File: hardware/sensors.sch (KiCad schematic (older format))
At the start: 22 parts

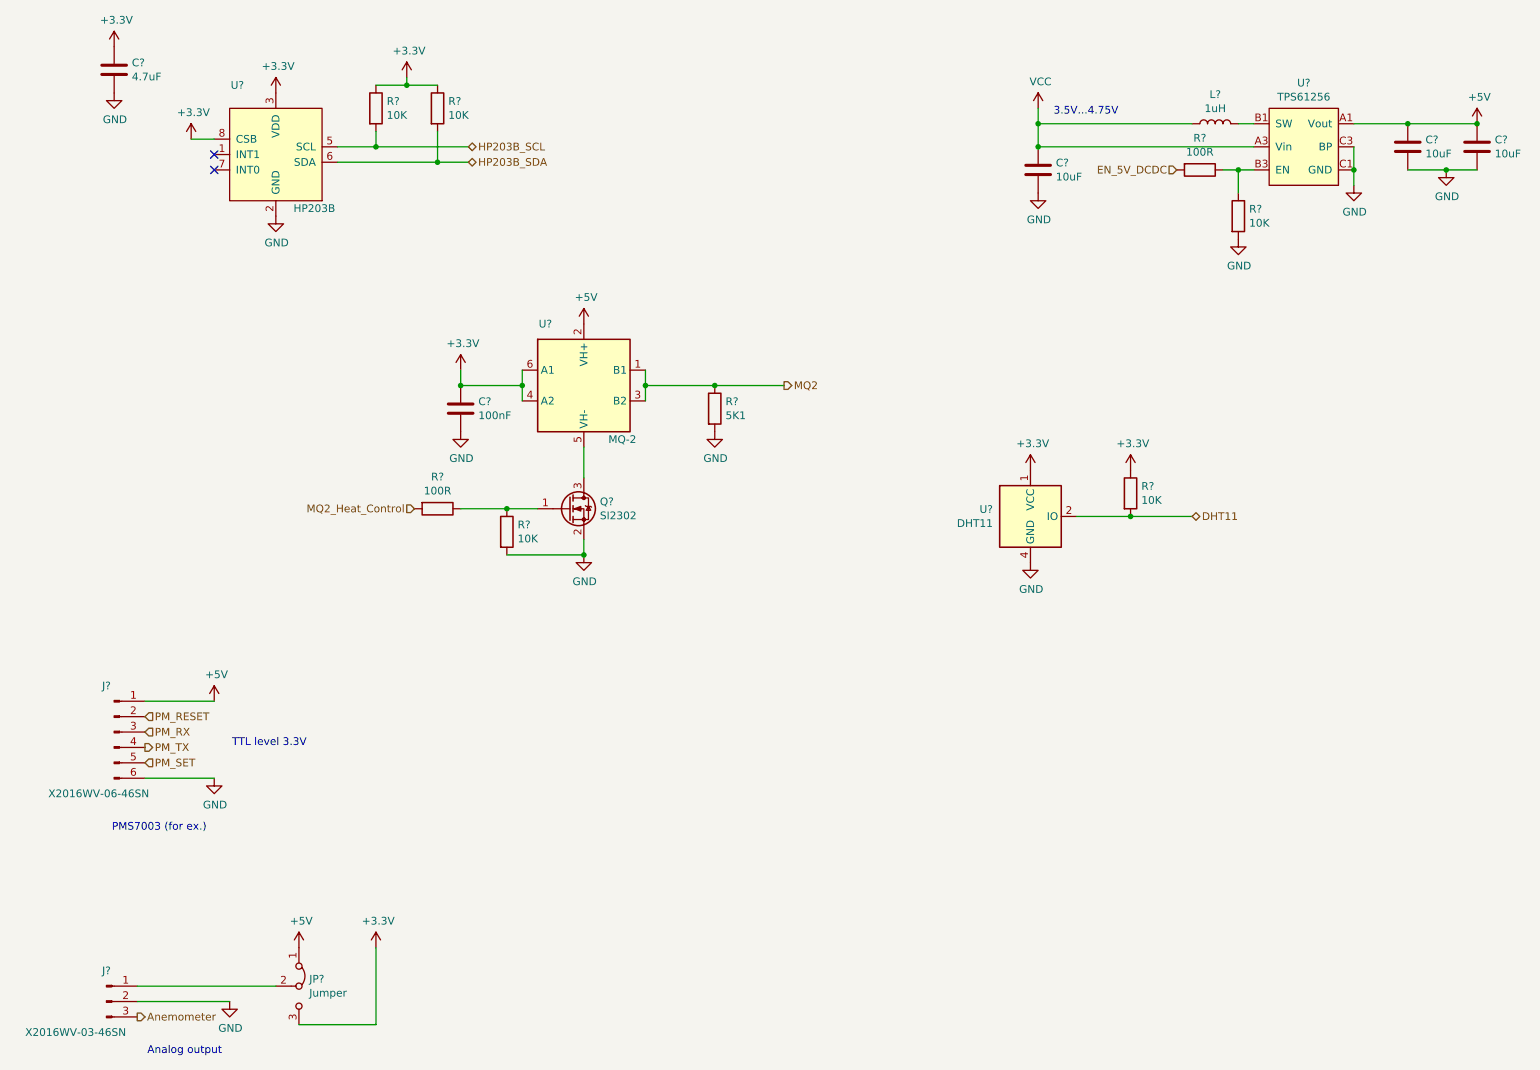
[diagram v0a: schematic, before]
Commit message: Select crystals, add HSE for stm32 and fixed some bits
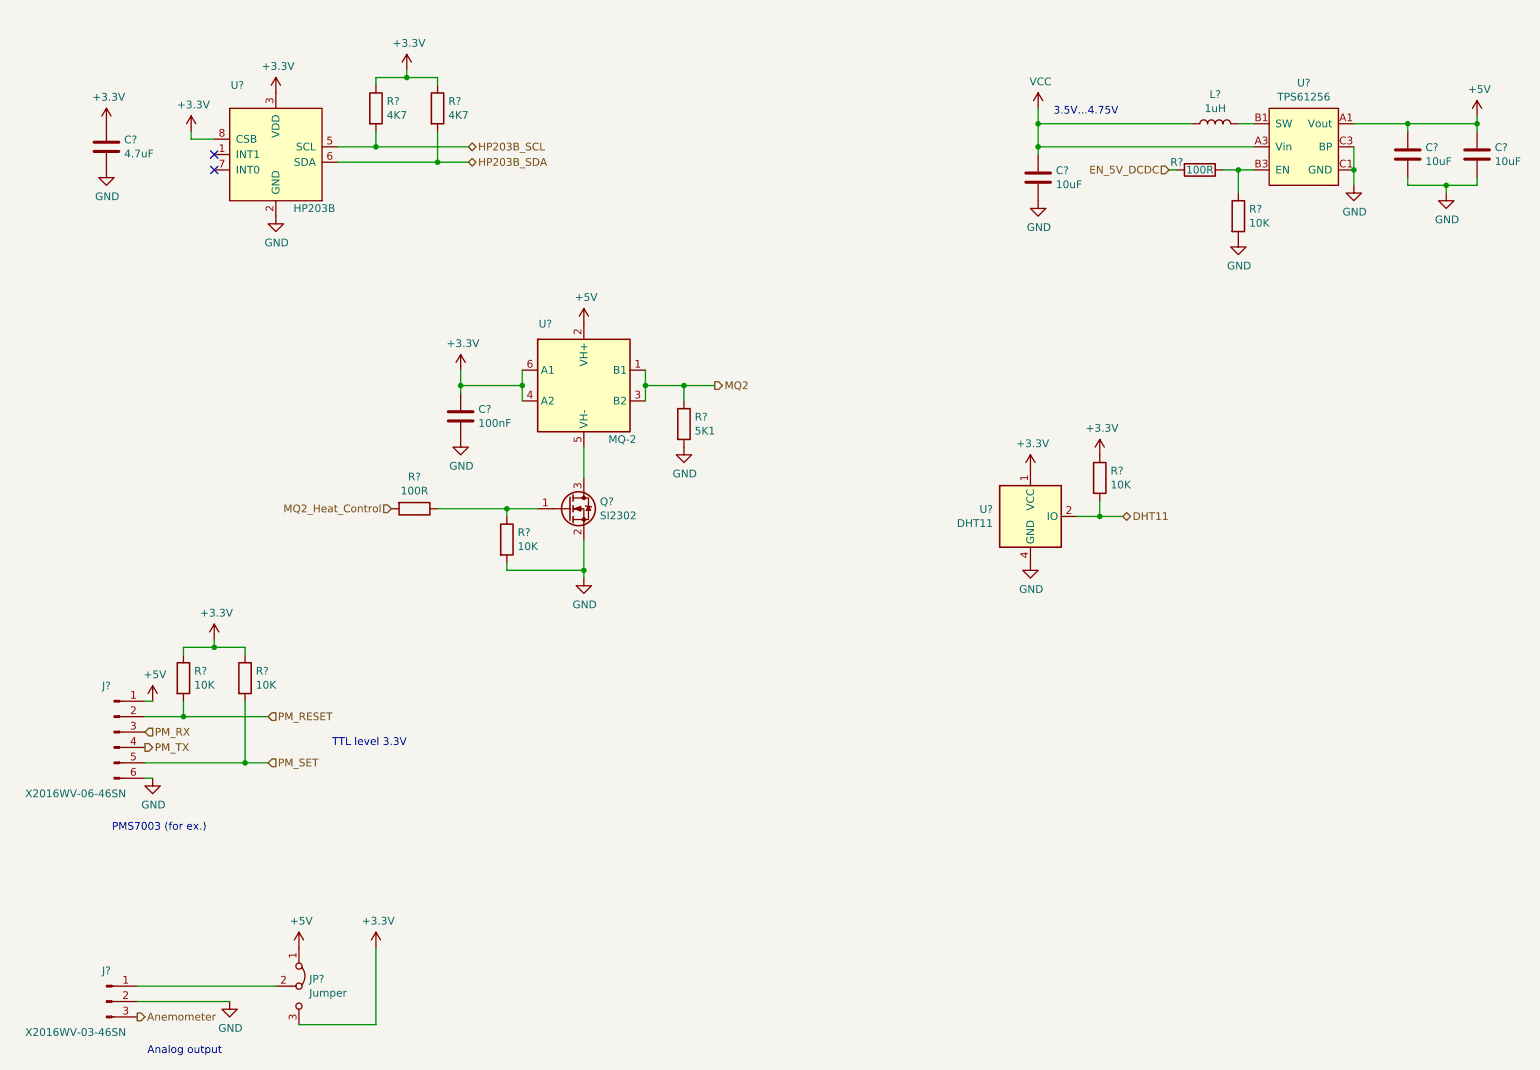
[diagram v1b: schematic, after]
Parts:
- added R? (x2): 10K, symbol Device:R
- R? (x2): value 10K -> 4K7
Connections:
- net +3V3: now also R?.1, R?.1
- net PM_RESET: now also R?.2
- net PM_SET: now also R?.2
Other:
- moved on the sheet: C?, R?

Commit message: Annotation complete
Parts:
- gave numbers to parts that had none: 24

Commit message: Finish adding footprints
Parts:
- removed U011: TPS61256, Package_BGA:Texas_DSBGA-9_1.4715x1.4715mm_Layout3x3_P0.5mm, symbol TPS61256:TPS61256
- C60, C61, C62, C63, C64: footprint (none) -> Capacitor_SMD:C_0805_2012Metric
- J3: value X2016WV-06-46SN -> PM_Sensor; footprint (none) -> Connector_PinSocket_2.00mm:PinSocket_1x06_P2.00mm_Vertical
- J4: value X2016WV-03-46SN -> Anemometer; footprint (none) -> Connector_PinSocket_2.00mm:PinSocket_1x03_P2.00mm_Vertical
- JP3: footprint (none) -> Connector_PinHeader_2.54mm:PinHeader_1x03_P2.54mm_Vertical
- L12: footprint (none) -> Inductor_SMD:L_0603_1608Metric
- R54, R55, R56, R57, R58, R59, R60, R61, R62, R63: footprint (none) -> Resistor_SMD:R_0805_2012Metric
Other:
- moved on the sheet: C63, R56
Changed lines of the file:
@@
 $EndComp
 $Comp
-L TPS61256:TPS61256 U011
+L TPS61256:TPS61256 #U011
 U 1 1 6059B871
 P 9050 1750
-F 0 "U011" H 9075 2165 50  0000 C CNN
+F 0 "#U011" H 9075 2165 50  0000 C CNN
 F 1 "TPS61256" H 9075 2074 50  0000 C CNN
 F 2 "Package_BGA:Texas_DSBGA-9_1.4715x1.4715mm_Layout3x3_P0.5mm" H 9050 2100 50  0001 C CNN
@@
 L power:VCC #PWR0105
 U 1 1 6059CBA1
-P 7350 1500
-F 0 "#PWR0105" H 7350 1350 50  0001 C CNN
-F 1 "VCC" H 7365 1673 50  0000 C CNN
-F 2 "" H 7350 1500 50  0001 C CNN
-F 3 "" H 7350 1500 50  0001 C CNN
-	1    7350 1500
+P 7200 1500
+F 0 "#PWR0105" H 7200 1350 50  0001 C CNN
+F 1 "VCC" H 7215 1673 50  0000 C CNN
+F 2 "" H 7200 1500 50  0001 C CNN
+F 3 "" H 7200 1500 50  0001 C CNN
+	1    7200 1500
 	1    0    0    -1
 $EndComp
@@
 F 0 "L12" V 8690 1600 50  0000 C CNN
 F 1 "1uH" V 8599 1600 50  0000 C CNN
-F 2 "" H 8500 1600 50  0001 C CNN
+F 2 "Inductor_SMD:L_0603_1608Metric" H 8500 1600 50  0001 C CNN
 F 3 "~" H 8500 1600 50  0001 C CNN
 	1    8500 1600
@@
 L Device:C C63
 U 1 1 6059E1D4
-P 7350 1950
-F 0 "C63" H 7465 1996 50  0000 L CNN
-F 1 "10uF" H 7465 1905 50  0000 L CNN
-F 2 "" H 7388 1800 50  0001 C CNN
-F 3 "~" H 7350 1950 50  0001 C CNN
-	1    7350 1950
+P 7200 1950
+F 0 "C63" H 7315 1996 50  0000 L CNN
+F 1 "10uF" H 7315 1905 50  0000 L CNN
+F 2 "Capacitor_SMD:C_0805_2012Metric" H 7238 1800 50  0001 C CNN
+F 3 "~" H 7200 1950 50  0001 C CNN
+	1    7200 1950
 	1    0    0    -1
 $EndComp
@@
 L power:GND #PWR0112
 U 1 1 605A030F
-P 7350 2100
-F 0 "#PWR0112" H 7350 1850 50  0001 C CNN
-F 1 "GND" H 7355 1927 50  0000 C CNN
-F 2 "" H 7350 2100 50  0001 C CNN
-F 3 "" H 7350 2100 50  0001 C CNN
-	1    7350 2100
+P 7200 2100
+F 0 "#PWR0112" H 7200 1850 50  0001 C CNN
+F 1 "GND" H 7205 1927 50  0000 C CNN
+F 2 "" H 7200 2100 50  0001 C CNN
+F 3 "" H 7200 2100 50  0001 C CNN
+	1    7200 2100
 	1    0    0    -1
 $EndComp
@@
 F 0 "C61" H 9865 1846 50  0000 L CNN
 F 1 "10uF" H 9865 1755 50  0000 L CNN
-F 2 "" H 9788 1650 50  0001 C CNN
+F 2 "Capacitor_SMD:C_0805_2012Metric" H 9788 1650 50  0001 C CNN
 F 3 "~" H 9750 1800 50  0001 C CNN
 	1    9750 1800
@@
 F 0 "C62" H 10315 1846 50  0000 L CNN
 F 1 "10uF" H 10315 1755 50  0000 L CNN
-F 2 "" H 10238 1650 50  0001 C CNN
+F 2 "Capacitor_SMD:C_0805_2012Metric" H 10238 1650 50  0001 C CNN
 F 3 "~" H 10200 1800 50  0001 C CNN
 	1    10200 1800
@@
 	1    0    0    -1
 $EndComp
-Text HLabel 8200 1900 0    50   Input ~ 0
+Text HLabel 8150 1900 0    50   Input ~ 0
 EN_5V_DCDC
 Wire Wire Line
-	7350 1750 7350 1600
-Connection ~ 7350 1750
-Connection ~ 7350 1600
-Wire Wire Line
-	7350 1600 7350 1500
+	7200 1750 7200 1600
+Connection ~ 7200 1750
+Connection ~ 7200 1600
+Wire Wire Line
+	7200 1600 7200 1500
 $Comp
 L Device:R R57
@@
 F 0 "R57" H 8720 2246 50  0000 L CNN
 F 1 "10K" H 8720 2155 50  0000 L CNN
-F 2 "" V 8580 2200 50  0001 C CNN
+F 2 "Resistor_SMD:R_0805_2012Metric" V 8580 2200 50  0001 C CNN
 F 3 "~" H 8650 2200 50  0001 C CNN
 	1    8650 2200
@@
 Wire Wire Line
 	8650 1900 8750 1900
-Wire Wire Line
-	8650 1900 8550 1900
-Connection ~ 8650 1900
-Text Notes 7450 1550 0    50   ~ 0
+Text Notes 7300 1550 0    50   ~ 0
 3.5V...4.75V
 $Comp
 L Device:R R56
 U 1 1 605B1BAE
-P 8400 1900
-F 0 "R56" V 8350 1750 50  0000 C CNN
-F 1 "100R" V 8400 1900 50  0000 C CNN
-F 2 "" V 8330 1900 50  0001 C CNN
-F 3 "~" H 8400 1900 50  0001 C CNN
-	1    8400 1900
+P 8450 1900
+F 0 "R56" V 8400 1700 50  0000 C CNN
+F 1 "100R" V 8450 1900 50  0000 C CNN
+F 2 "Resistor_SMD:R_0805_2012Metric" V 8380 1900 50  0001 C CNN
+F 3 "~" H 8450 1900 50  0001 C CNN
+	1    8450 1900
 	0    1    1    0
 $EndComp
-Wire Wire Line
-	7350 1750 8750 1750
-Wire Wire Line
-	7350 1600 8350 1600
 $Comp
 L Connector:Conn_01x06_Male J3
@@
 P 1350 5550
 F 0 "J3" H 1300 5850 50  0000 C CNN
-F 1 "X2016WV-06-46SN" H 1100 5150 50  0000 C CNN
-F 2 "" H 1350 5550 50  0001 C CNN
+F 1 "PM_Sensor" H 1300 5150 50  0000 C CNN
+F 2 "Connector_PinSocket_2.00mm:PinSocket_1x06_P2.00mm_Vertical" H 1350 5550 50  0001 C CNN
 F 3 "~" H 1350 5550 50  0001 C CNN
 	1    1350 5550
@@
 F 0 "C60" H 1415 1796 50  0000 L CNN
 F 1 "4.7uF" H 1415 1705 50  0000 L CNN
-F 2 "" H 1338 1600 50  0001 C CNN
+F 2 "Capacitor_SMD:C_0805_2012Metric" H 1338 1600 50  0001 C CNN
 F 3 "~" H 1300 1750 50  0001 C CNN
 	1    1300 1750
@@
 F 0 "R54" H 3120 1546 50  0000 L CNN
 F 1 "4K7" H 3120 1455 50  0000 L CNN
-F 2 "" V 2980 1500 50  0001 C CNN
+F 2 "Resistor_SMD:R_0805_2012Metric" V 2980 1500 50  0001 C CNN
 F 3 "~" H 3050 1500 50  0001 C CNN
 	1    3050 1500
@@
 F 0 "R55" H 3520 1546 50  0000 L CNN
 F 1 "4K7" H 3520 1455 50  0000 L CNN
-F 2 "" V 3380 1500 50  0001 C CNN
+F 2 "Resistor_SMD:R_0805_2012Metric" V 3380 1500 50  0001 C CNN
 F 3 "~" H 3450 1500 50  0001 C CNN
 	1    3450 1500
@@
 F 0 "R59" H 7820 3946 50  0000 L CNN
 F 1 "10K" H 7820 3855 50  0000 L CNN
-F 2 "" V 7680 3900 50  0001 C CNN
+F 2 "Resistor_SMD:R_0805_2012Metric" V 7680 3900 50  0001 C CNN
 F 3 "~" H 7750 3900 50  0001 C CNN
 	1    7750 3900
@@
 F 0 "R58" H 5120 3596 50  0000 L CNN
 F 1 "5K1" H 5120 3505 50  0000 L CNN
-F 2 "" V 4980 3550 50  0001 C CNN
+F 2 "Resistor_SMD:R_0805_2012Metric" V 4980 3550 50  0001 C CNN
 F 3 "~" H 5050 3550 50  0001 C CNN
 	1    5050 3550
@@
 P 1300 7300
 F 0 "J4" H 1300 7500 50  0000 C CNN
-F 1 "X2016WV-03-46SN" H 1100 7100 50  0000 C CNN
-F 2 "" H 1300 7300 50  0001 C CNN
+F 1 "Anemometer" H 1300 7100 50  0000 C CNN
+F 2 "Connector_PinSocket_2.00mm:PinSocket_1x03_P2.00mm_Vertical" H 1300 7300 50  0001 C CNN
 F 3 "~" H 1300 7300 50  0001 C CNN
 	1    1300 7300
@@
 F 0 "JP3" V 2504 7267 50  0000 L CNN
 F 1 "Jumper" V 2595 7267 50  0000 L CNN
-F 2 "" H 2550 7200 50  0001 C CNN
+F 2 "Connector_PinHeader_2.54mm:PinHeader_1x03_P2.54mm_Vertical" H 2550 7200 50  0001 C CNN
 F 3 "~" H 2550 7200 50  0001 C CNN
 	1    2550 7200
@@
 F 0 "C64" H 3715 3546 50  0000 L CNN
 F 1 "100nF" H 3715 3455 50  0000 L CNN
-F 2 "" H 3638 3350 50  0001 C CNN
+F 2 "Capacitor_SMD:C_0805_2012Metric" H 3638 3350 50  0001 C CNN
 F 3 "~" H 3600 3500 50  0001 C CNN
 	1    3600 3500
@@
 	1    0    0    -1
 $EndComp
-Wire Wire Line
-	4400 3700 4400 3900
 $Comp
 L Device:R R61
@@
 F 0 "R61" H 3970 4346 50  0000 L CNN
 F 1 "10K" H 3970 4255 50  0000 L CNN
-F 2 "" V 3830 4300 50  0001 C CNN
+F 2 "Resistor_SMD:R_0805_2012Metric" V 3830 4300 50  0001 C CNN
 F 3 "~" H 3900 4300 50  0001 C CNN
 	1    3900 4300
@@
 F 0 "R60" V 3093 4100 50  0000 C CNN
 F 1 "100R" V 3184 4100 50  0000 C CNN
-F 2 "" V 3230 4100 50  0001 C CNN
+F 2 "Resistor_SMD:R_0805_2012Metric" V 3230 4100 50  0001 C CNN
 F 3 "~" H 3300 4100 50  0001 C CNN
 	1    3300 4100
@@
 F 0 "R62" H 1870 5246 50  0000 L CNN
 F 1 "10K" H 1870 5155 50  0000 L CNN
-F 2 "" V 1730 5200 50  0001 C CNN
+F 2 "Resistor_SMD:R_0805_2012Metric" V 1730 5200 50  0001 C CNN
 F 3 "~" H 1800 5200 50  0001 C CNN
 	1    1800 5200
@@
 F 0 "R63" H 2270 5246 50  0000 L CNN
 F 1 "10K" H 2270 5155 50  0000 L CNN
-F 2 "" V 2130 5200 50  0001 C CNN
+F 2 "Resistor_SMD:R_0805_2012Metric" V 2130 5200 50  0001 C CNN
 F 3 "~" H 2200 5200 50  0001 C CNN
 	1    2200 5200
@@
 	7750 4150 7900 4150
 Wire Wire Line
-	8200 1900 8250 1900
-Wire Wire Line
 	9400 1600 9750 1600
 Wire Wire Line
@@
 	10000 2000 10200 2000
 Wire Wire Line
-	7350 1800 7350 1750
+	7200 1800 7200 1750
 Wire Wire Line
 	1850 1700 1850 1650
+Wire Wire Line
+	4400 3700 4400 3900
+Wire Wire Line
+	8600 1900 8650 1900
+Connection ~ 8650 1900
+Wire Wire Line
+	7200 1750 8750 1750
+Wire Wire Line
+	7200 1600 8350 1600
+Wire Wire Line
+	8150 1900 8300 1900
 $EndSCHEMATC

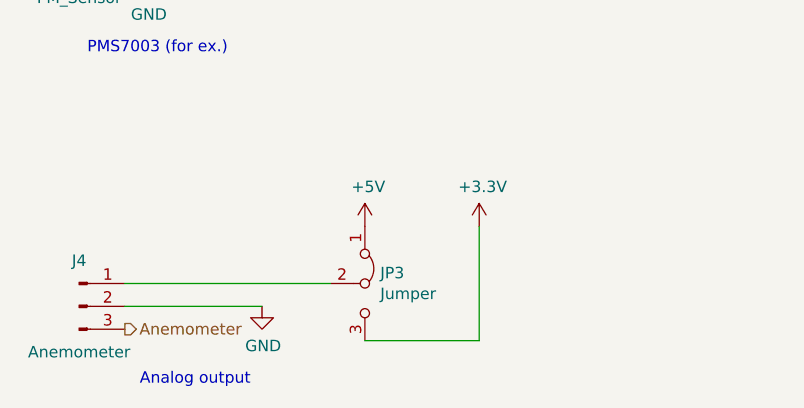
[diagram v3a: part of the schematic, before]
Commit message: Change 0Rto solder jumpers Add 3d model for bq25895 Fix button pcb model Start power part of pcb
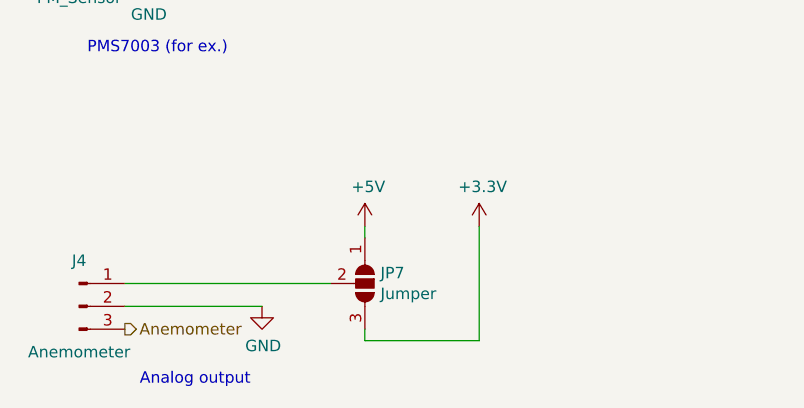
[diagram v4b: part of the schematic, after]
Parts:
- removed JP3: Jumper, Connector_PinHeader_2.54mm:PinHeader_1x03_P2.54mm_Vertical, symbol Jumper:Jumper_3_Bridged12
- added JP7: Jumper, Jumper:SolderJumper-3_P1.3mm_Open_Pad1.0x1.5mm_NumberLabels, symbol Jumper:SolderJumper_3_Open
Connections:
- net +3V3: now also JP7.3 (B)
- net +5V: now also JP7.1 (A)
- net at J4.1 (Pin_1): now also JP7.2 (C)
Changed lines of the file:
@@
 	2400 7200 1500 7200
-$Comp
-L Jumper:Jumper_3_Bridged12 JP3
-U 1 1 605CBA25
-P 2550 7200
-F 0 "JP3" V 2504 7267 50  0000 L CNN
-F 1 "Jumper" V 2595 7267 50  0000 L CNN
-F 2 "Connector_PinHeader_2.54mm:PinHeader_1x03_P2.54mm_Vertical" H 2550 7200 50  0001 C CNN
-F 3 "~" H 2550 7200 50  0001 C CNN
-	1    2550 7200
-	0    1    1    0
-$EndComp
 $Comp
 L power:+3.3V #PWR0127
@@
 Wire Wire Line
 	8150 1900 8300 1900
+$Comp
+L Jumper:SolderJumper_3_Open JP7
+U 1 1 608E12BC
+P 2550 7200
+F 0 "JP7" V 2504 7268 50  0000 L CNN
+F 1 "Jumper" V 2595 7268 50  0000 L CNN
+F 2 "Jumper:SolderJumper-3_P1.3mm_Open_Pad1.0x1.5mm_NumberLabels" H 2550 7200 50  0001 C CNN
+F 3 "~" H 2550 7200 50  0001 C CNN
+	1    2550 7200
+	0    1    1    0
+$EndComp
+Wire Wire Line
+	2550 6950 2550 7000
+Wire Wire Line
+	2550 7450 2550 7400
 $EndSCHEMATC
